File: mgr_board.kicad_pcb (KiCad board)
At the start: 2 copper layers, 150 x 150 mm, 280 parts, among them IC1 MCP48CVB08-20E_ST, IC10 A6214KLKTR-T, IC11 A6214KLKTR-T, IC12 A6214KLKTR-T, IC13 A6214KLKTR-T, IC2 A6214KLKTR-T, IC3 A6214KLKTR-T, IC4 A6214KLKTR-T, IC5 A6214KLKTR-T, IC6 A6214KLKTR-T, IC7 A6214KLKTR-T, IC8 A6214KLKTR-T, IC9 A6214KLKTR-T, J1 Screw_Terminal_2_P5.00mm, J3 SD Card SPI Module, J4 Micro_SD_Card, U1 TPS562201DDCR, U10 INA180A1, U11 INA180A1, U12 INA180A1, U13 INA180A1, U14 INA180A1, U2 LM2596 BUCK MODULE, U3 INA180A1, U4 INA180A1, U5 INA180A1, U6 INA180A1, U7 INA180A1, U8 INA180A1, U9 INA180A1

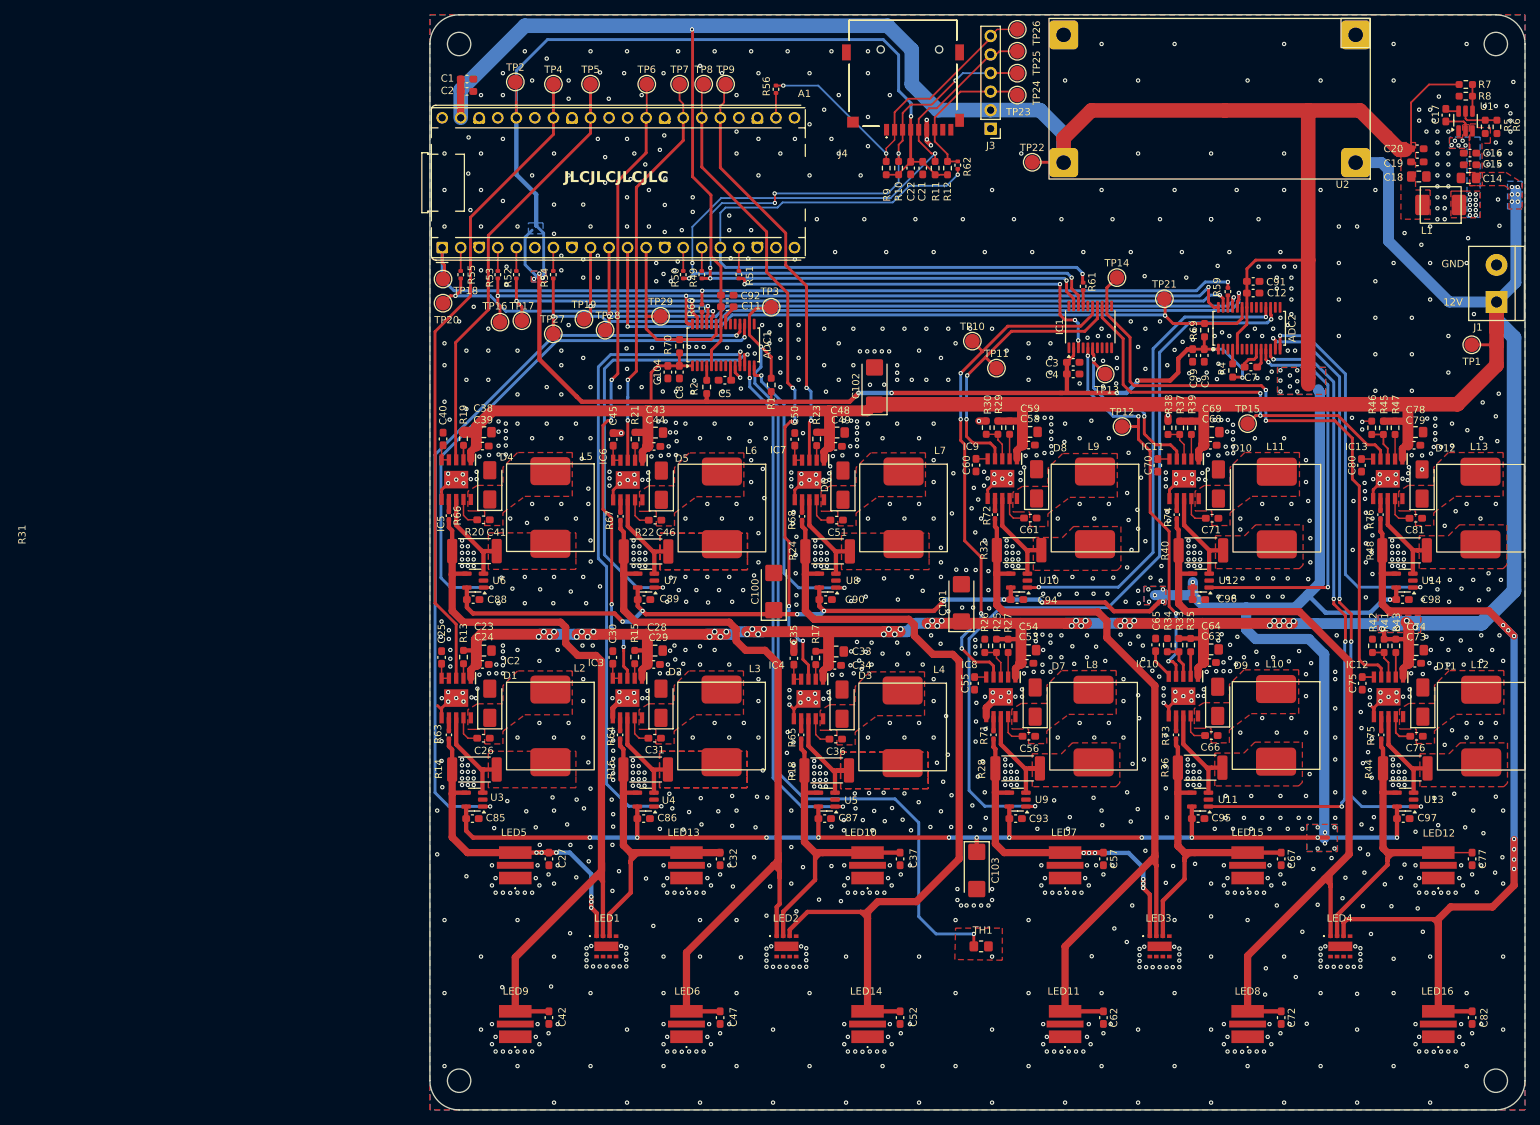
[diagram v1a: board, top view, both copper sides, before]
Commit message: Added low pass filters at current sense amp outputs and pull ups on cs pins, DRC done
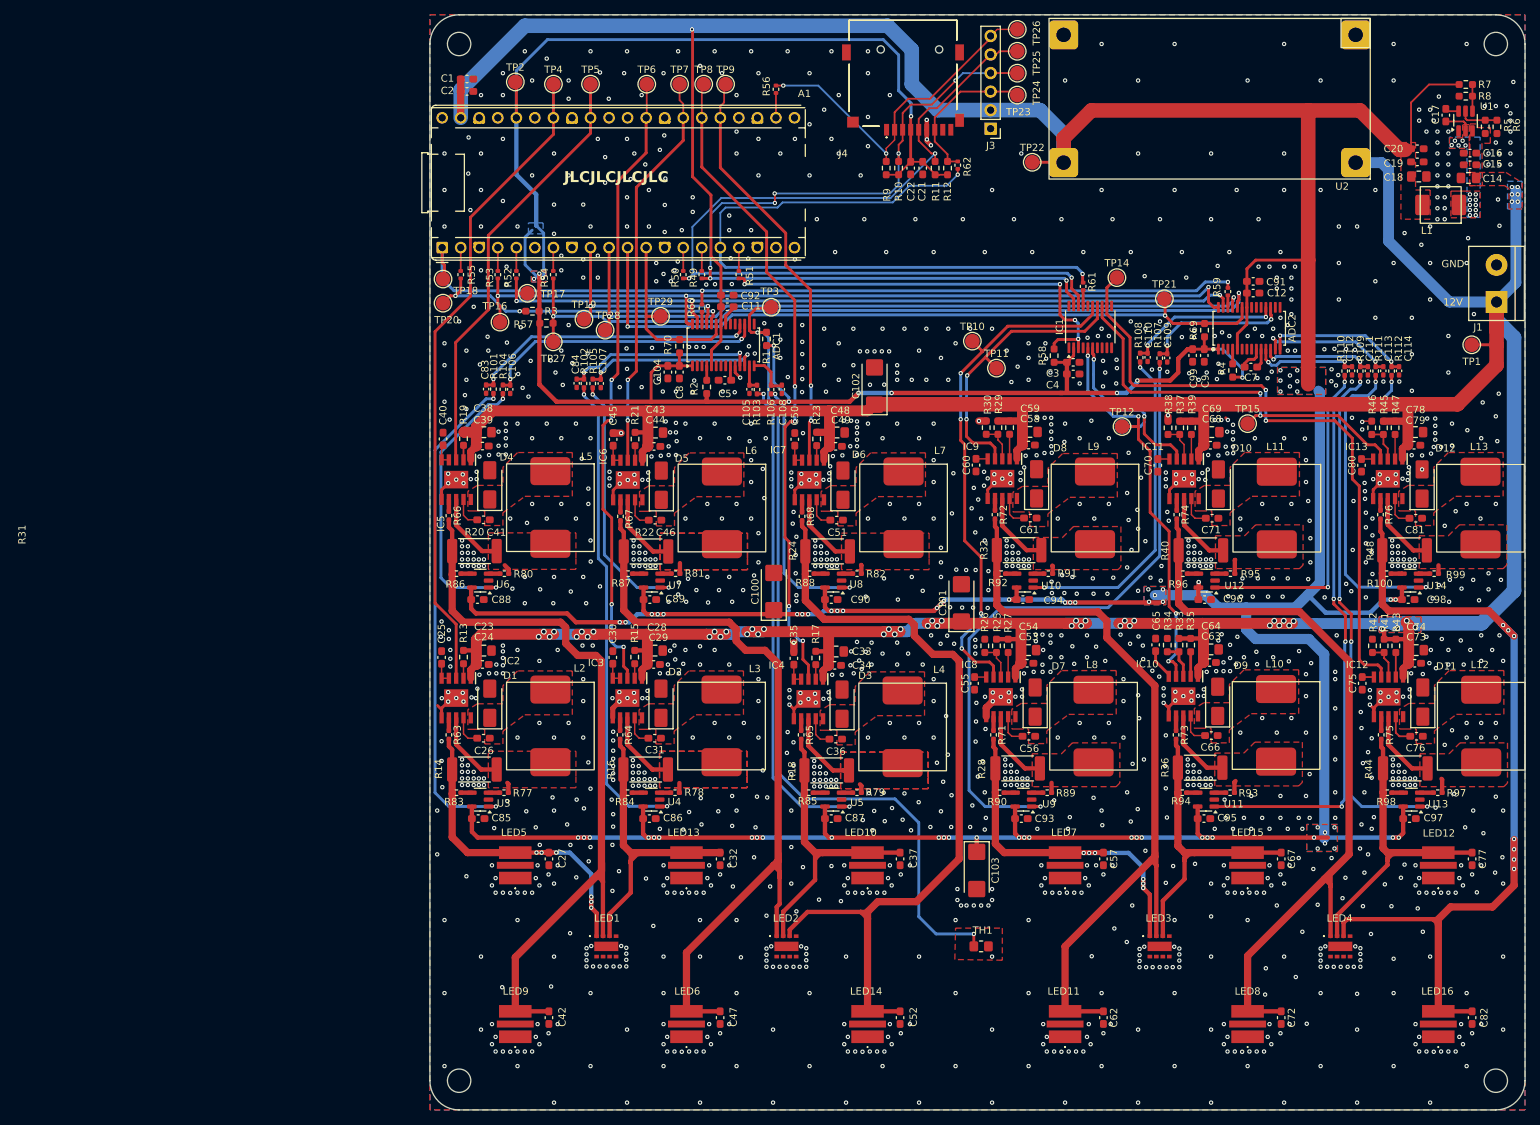
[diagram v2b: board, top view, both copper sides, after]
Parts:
- added C105: 1nF, Capacitor_SMD:C_0402_1005Metric_Pad0.74x0.62mm_HandSolder, F.Cu at (61.8, 72.3)
- added C106: 1nF, Capacitor_SMD:C_0402_1005Metric_Pad0.74x0.62mm_HandSolder, F.Cu at (29.0, 72.3)
- added C107: 1nF, Capacitor_SMD:C_0402_1005Metric_Pad0.74x0.62mm_HandSolder, F.Cu at (41.4, 71.5)
- added C108: 1nF, Capacitor_SMD:C_0402_1005Metric_Pad0.74x0.62mm_HandSolder, F.Cu at (66.2, 72.3)
- added C109: 1nF, Capacitor_SMD:C_0402_1005Metric_Pad0.74x0.62mm_HandSolder, F.Cu at (119.0, 68.0)
- added C110: 1nF, Capacitor_SMD:C_0402_1005Metric_Pad0.74x0.62mm_HandSolder, F.Cu at (116.3, 67.9)
- added C111: 1nF, Capacitor_SMD:C_0402_1005Metric_Pad0.74x0.62mm_HandSolder, F.Cu at (146.5, 69.8)
- added C112: 1nF, Capacitor_SMD:C_0402_1005Metric_Pad0.74x0.62mm_HandSolder, F.Cu at (144.3, 69.8)
- added C113: 1nF, Capacitor_SMD:C_0402_1005Metric_Pad0.74x0.62mm_HandSolder, F.Cu at (148.6, 69.8)
- added C114: 1nF, Capacitor_SMD:C_0402_1005Metric_Pad0.74x0.62mm_HandSolder, F.Cu at (150.7, 69.8)
- added C83: 1nF, Capacitor_SMD:C_0402_1005Metric_Pad0.74x0.62mm_HandSolder, F.Cu at (25.7, 72.3)
- added C84: 1nF, Capacitor_SMD:C_0402_1005Metric_Pad0.74x0.62mm_HandSolder, F.Cu at (38.1, 71.5)
- added R100: 0R, Resistor_SMD:R_0402_1005Metric_Pad0.72x0.64mm_HandSolder, F.Cu at (149.0, 97.5)
- added R101: 1,5k, Resistor_SMD:R_0402_1005Metric_Pad0.72x0.64mm_HandSolder, F.Cu at (26.7, 72.3)
- added R102: 1,5k, Resistor_SMD:R_0402_1005Metric_Pad0.72x0.64mm_HandSolder, F.Cu at (39.1, 71.5)
- added R103: 1,5k, Resistor_SMD:R_0402_1005Metric_Pad0.72x0.64mm_HandSolder, F.Cu at (62.8, 72.3)
- added R104: 1,5k, Resistor_SMD:R_0402_1005Metric_Pad0.72x0.64mm_HandSolder, F.Cu at (28.0, 72.3)
- added R105: 1,5k, Resistor_SMD:R_0402_1005Metric_Pad0.72x0.64mm_HandSolder, F.Cu at (40.3, 71.5)
- added R106: 1,5k, Resistor_SMD:R_0402_1005Metric_Pad0.72x0.64mm_HandSolder, F.Cu at (64.7, 72.3)
- added R107: 1,5k, Resistor_SMD:R_0402_1005Metric_Pad0.72x0.64mm_HandSolder, F.Cu at (118.0, 68.0)
- added R108: 1,5k, Resistor_SMD:R_0402_1005Metric_Pad0.72x0.64mm_HandSolder, F.Cu at (115.3, 68.0)
- added R109: 1,5k, Resistor_SMD:R_0402_1005Metric_Pad0.72x0.64mm_HandSolder, F.Cu at (145.4, 69.8)
- added R110: 1,5k, Resistor_SMD:R_0402_1005Metric_Pad0.72x0.64mm_HandSolder, F.Cu at (143.3, 69.8)
- added R111: 1,5k, Resistor_SMD:R_0402_1005Metric_Pad0.72x0.64mm_HandSolder, F.Cu at (147.5, 69.8)
- added R112: 1,5k, Resistor_SMD:R_0402_1005Metric_Pad0.72x0.64mm_HandSolder, F.Cu at (149.7, 69.8)
- added R3: 10k, Resistor_SMD:R_0603_1608Metric_Pad0.98x0.95mm_HandSolder, F.Cu at (32.0, 61.6)
- added R57: 10k, Resistor_SMD:R_0603_1608Metric_Pad0.98x0.95mm_HandSolder, F.Cu at (34.0, 63.2)
- added R58: 10k, Resistor_SMD:R_0603_1608Metric_Pad0.98x0.95mm_HandSolder, F.Cu at (103.5, 67.7)
- added R77: 0R, Resistor_SMD:R_0402_1005Metric_Pad0.72x0.64mm_HandSolder, F.Cu at (28.1, 127.5)
- added R78: 0R, Resistor_SMD:R_0402_1005Metric_Pad0.72x0.64mm_HandSolder, F.Cu at (51.6, 127.5)
- added R79: 0R, Resistor_SMD:R_0402_1005Metric_Pad0.72x0.64mm_HandSolder, F.Cu at (76.5, 127.5)
- added R80: 0R, Resistor_SMD:R_0402_1005Metric_Pad0.72x0.64mm_HandSolder, F.Cu at (28.2, 97.5)
- added R81: 0R, Resistor_SMD:R_0402_1005Metric_Pad0.72x0.64mm_HandSolder, F.Cu at (51.6, 97.5)
- added R82: 0R, Resistor_SMD:R_0402_1005Metric_Pad0.72x0.64mm_HandSolder, F.Cu at (76.5, 97.5)
- added R83: 0R, Resistor_SMD:R_0402_1005Metric_Pad0.72x0.64mm_HandSolder, F.Cu at (21.6, 127.5)
- added R84: 0R, Resistor_SMD:R_0402_1005Metric_Pad0.72x0.64mm_HandSolder, F.Cu at (45.1, 127.5)
- added R85: 0R, Resistor_SMD:R_0402_1005Metric_Pad0.72x0.64mm_HandSolder, F.Cu at (69.9, 127.5)
- added R86: 0R, Resistor_SMD:R_0402_1005Metric_Pad0.72x0.64mm_HandSolder, F.Cu at (21.6, 97.5)
- added R87: 0R, Resistor_SMD:R_0402_1005Metric_Pad0.72x0.64mm_HandSolder, F.Cu at (45.1, 97.5)
- added R88: 0R, Resistor_SMD:R_0402_1005Metric_Pad0.72x0.64mm_HandSolder, F.Cu at (70.0, 97.5)
- added R89: 0R, Resistor_SMD:R_0402_1005Metric_Pad0.72x0.64mm_HandSolder, F.Cu at (102.5, 127.5)
- added R90: 0R, Resistor_SMD:R_0402_1005Metric_Pad0.72x0.64mm_HandSolder, F.Cu at (96.0, 127.5)
- added R91: 0R, Resistor_SMD:R_0402_1005Metric_Pad0.72x0.64mm_HandSolder, F.Cu at (102.7, 97.5)
- added R92: 0R, Resistor_SMD:R_0402_1005Metric_Pad0.72x0.64mm_HandSolder, F.Cu at (96.2, 97.5)
- added R93: 0R, Resistor_SMD:R_0402_1005Metric_Pad0.72x0.64mm_HandSolder, F.Cu at (127.6, 127.5)
- added R94: 0R, Resistor_SMD:R_0402_1005Metric_Pad0.72x0.64mm_HandSolder, F.Cu at (121.0, 127.5)
- added R95: 0R, Resistor_SMD:R_0402_1005Metric_Pad0.72x0.64mm_HandSolder, F.Cu at (127.7, 97.5)
- added R96: 0R, Resistor_SMD:R_0402_1005Metric_Pad0.72x0.64mm_HandSolder, F.Cu at (121.1, 97.5)
- added R97: 0R, Resistor_SMD:R_0402_1005Metric_Pad0.72x0.64mm_HandSolder, F.Cu at (156.1, 127.5)
- added R98: 0R, Resistor_SMD:R_0402_1005Metric_Pad0.72x0.64mm_HandSolder, F.Cu at (149.1, 127.5)
- added R99: 0R, Resistor_SMD:R_0402_1005Metric_Pad0.72x0.64mm_HandSolder, F.Cu at (155.5, 97.5)
- R63, R64, R65, R66, R67, R68, R71, R72, R73, R74, R75, R76: footprint Capacitor_SMD:C_0402_1005Metric_Pad0.74x0.62mm_HandSolder -> Resistor_SMD:R_0402_1005Metric_Pad0.72x0.64mm_HandSolder
- TP13: moved to B.Cu
- moved TP13 7.56 mm to (112.8, 77.4), turned to 180 degrees
- moved R1 6.33 mm to (64.1, 65.4)
- moved TP17 3.82 mm to (31.4, 59.1)
- moved TP27 1.10 mm to (34.9, 65.8)
- moved U5 0.90 mm to (73.2, 128.5)
- moved C87 0.90 mm to (73.0, 131.1)
- moved C97 0.85 mm to (152.2, 131.1)
- moved U13 0.85 mm to (152.4, 128.5)
- moved C95 0.80 mm to (124.0, 131.1)
- moved U12 0.80 mm to (124.4, 98.5)
- moved C89 0.80 mm to (48.1, 101.1)
- moved C94 0.80 mm to (99.2, 101.1)
- moved C96 0.80 mm to (124.1, 101.1)
- moved U10 0.80 mm to (99.5, 98.5)
- moved U11 0.80 mm to (124.3, 128.5)
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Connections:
- U10 pad 1: /ADCs/LED_CURR_7 -> Net-(R108-Pad1)
- U10 pad 3: Net-(IC9-CSH) -> Net-(U10-+)
- U10 pad 4: /LED_LOAD_7 -> Net-(U10--)
- U11 pad 1: /ADCs/LED_CURR_8 -> Net-(R109-Pad1)
- U11 pad 3: Net-(IC10-CSH) -> Net-(U11-+)
- U11 pad 4: /LED_LOAD_8 -> Net-(U11--)
- U12 pad 1: /ADCs/LED_CURR_9 -> Net-(R110-Pad1)
- U12 pad 3: Net-(IC11-CSH) -> Net-(U12-+)
- U12 pad 4: /LED_LOAD_9 -> Net-(U12--)
- U13 pad 1: /ADCs/LED_CURR_10 -> Net-(R111-Pad1)
- U13 pad 3: Net-(IC12-CSH) -> Net-(U13-+)
- U13 pad 4: /LED_LOAD_10 -> Net-(U13--)
- U14 pad 1: /ADCs/LED_CURR_11 -> Net-(R112-Pad1)
- U14 pad 3: Net-(IC13-CSH) -> Net-(U14-+)
- U14 pad 4: /LED_LOAD_11 -> Net-(U14--)
- U3 pad 1: /ADCs/LED_CURR_0 -> Net-(R101-Pad1)
- U3 pad 3: Net-(IC2-CSH) -> Net-(U3-+)
- U3 pad 4: /LED_LOAD_0 -> Net-(U3--)
- U4 pad 1: /ADCs/LED_CURR_2 -> Net-(R102-Pad1)
- U4 pad 3: Net-(IC3-CSH) -> Net-(U4-+)
- U4 pad 4: /LED_LOAD_2 -> Net-(U4--)
- U5 pad 1: /ADCs/LED_CURR_4 -> Net-(R103-Pad1)
- U5 pad 3: Net-(IC4-CSH) -> Net-(U5-+)
- U5 pad 4: /LED_LOAD_4 -> Net-(U5--)
- U6 pad 1: /ADCs/LED_CURR_1 -> Net-(R104-Pad1)
- U6 pad 3: Net-(IC5-CSH) -> Net-(U6-+)
- U6 pad 4: /LED_LOAD_1 -> Net-(U6--)
- U7 pad 1: /ADCs/LED_CURR_3 -> Net-(R105-Pad1)
- U7 pad 3: Net-(IC6-CSH) -> Net-(U7-+)
- U7 pad 4: /LED_LOAD_3 -> Net-(U7--)
- U8 pad 1: /ADCs/LED_CURR_5 -> Net-(R106-Pad1)
- U8 pad 3: Net-(IC7-CSH) -> Net-(U8-+)
- U8 pad 4: /LED_LOAD_5 -> Net-(U8--)
- U9 pad 1: /ADCs/LED_CURR_6 -> Net-(R107-Pad1)
- U9 pad 3: Net-(IC8-CSH) -> Net-(U9-+)
- U9 pad 4: /LED_LOAD_6 -> Net-(U9--)
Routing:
- net Net-(R107-Pad1): track 0.00 -> 90.0 mm, vias 0 -> 2
- net /ADCs/LED_CURR_6: track 109.5 -> 20.3 mm
- net Net-(R109-Pad1): track 0.00 -> 79.3 mm, vias 0 -> 4
- net Net-(R111-Pad1): track 0.00 -> 73.6 mm, vias 0 -> 4
- net /ADCs/LED_CURR_8: track 88.5 -> 15.7 mm, vias 4 -> 2
- net Net-(R101-Pad1): track 0.00 -> 68.7 mm, vias 0 -> 2
- net Net-(R103-Pad1): track 0.00 -> 67.2 mm, vias 0 -> 2
- net /ADCs/LED_CURR_4: track 70.1 -> 3.69 mm, vias 2 -> 0
- net Net-(R102-Pad1): track 0.00 -> 66.1 mm, vias 0 -> 2
- net /ADCs/LED_CURR_0: track 105.5 -> 39.6 mm
- net /ADCs/LED_CURR_2: track 89.8 -> 26.3 mm
- net /ADCs/LED_CURR_10: track 82.2 -> 18.8 mm, vias 4 -> 2
- net Net-(R108-Pad1): track 0.00 -> 45.5 mm, vias 0 -> 2
- net Net-(R110-Pad1): track 0.00 -> 45.5 mm, vias 0 -> 2
- net Net-(R112-Pad1): track 0.00 -> 44.8 mm, vias 0 -> 2
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
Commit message: fixed some kutases
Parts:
- moved TP16 0.30 mm to (27.3, 63.1)
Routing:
- net /SPI1_MISO: track 93.8 -> 81.1 mm, vias 2 -> 3
- net /SPI1_SCL: track 126.3 -> 114.7 mm, vias 3 -> 4
- net /SPI1_MOSI: track 120.1 -> 113.1 mm, vias 7 -> 5
- net GND: track 55.8 -> 61.1 mm, vias 1626 -> 1621
